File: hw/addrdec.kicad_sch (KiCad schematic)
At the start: 5 parts, among them U10 74AS138, U11 74ACT00P, U5 74AHCT02, U8 74AS04N, U9 74AS27

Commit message: add hw design for veraduino
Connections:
- net DEV0_~{CS} renamed VERA_~{CS}
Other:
- moved on the sheet: U11C, U11E, U5D, U8A, U8G, U9C, U9D

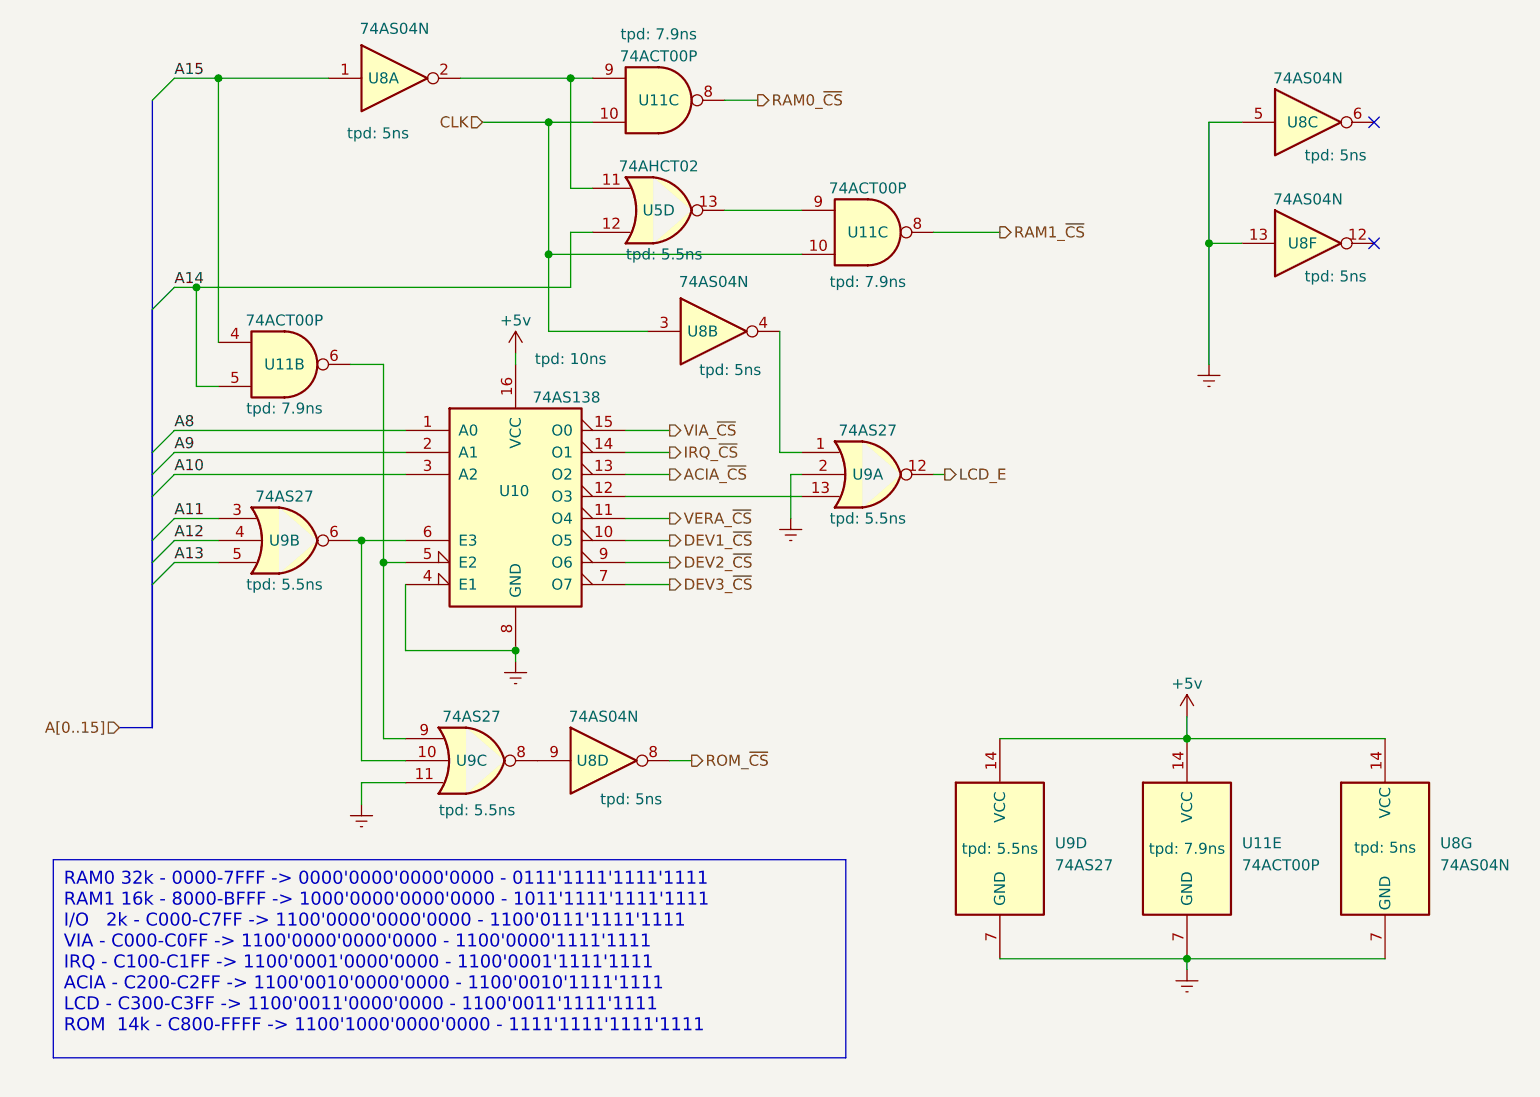
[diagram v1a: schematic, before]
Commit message: add hw schematics for video output with veraduino
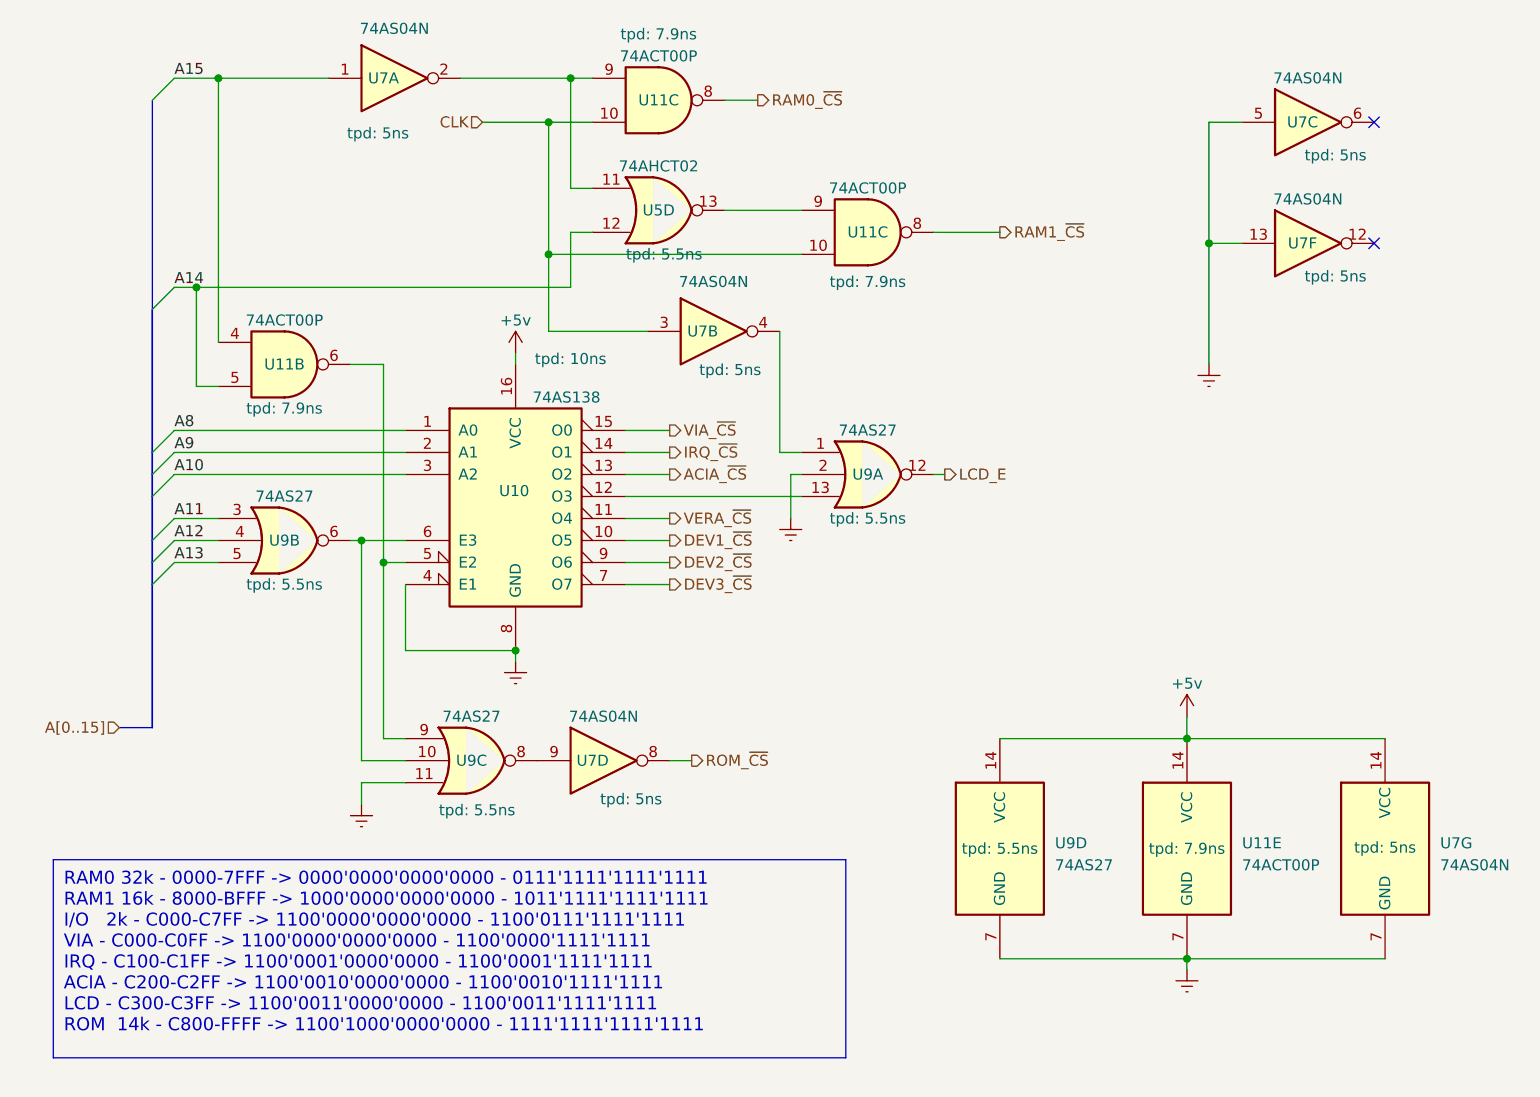
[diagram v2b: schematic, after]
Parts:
- renumbered U8 to U7
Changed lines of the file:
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@@
   (symbol (lib_id "74xx:74LS04") (at 161.29 43.18 0) (unit 6)
     (in_bom yes) (on_board yes) (dnp no)
-    (property "Reference" "U8" (at 160.655 43.18 0)
+    (property "Reference" "U7" (at 160.655 43.18 0)
       (effects (font (size 1.27 1.27)))
     )
@@
       (project "rod6502"
         (path "/031ea57b-8d17-4b45-87cc-c58302485ce1/4032fa43-c28c-4c35-b0ce-d5d9da6e84af"
-          (reference "U8") (unit 6)
+          (reference "U7") (unit 6)
         )
         (path "/031ea57b-8d17-4b45-87cc-c58302485ce1/890f0003-2042-459e-ac4a-1dd81f8fbcc6"
@@
   (symbol (lib_id "74xx:74LS04") (at 161.29 29.21 0) (unit 3)
     (in_bom yes) (on_board yes) (dnp no)
-    (property "Reference" "U8" (at 160.655 29.21 0)
+    (property "Reference" "U7" (at 160.655 29.21 0)
       (effects (font (size 1.27 1.27)))
     )
@@
       (project "rod6502"
         (path "/031ea57b-8d17-4b45-87cc-c58302485ce1/4032fa43-c28c-4c35-b0ce-d5d9da6e84af"
-          (reference "U8") (unit 3)
+          (reference "U7") (unit 3)
         )
         (path "/031ea57b-8d17-4b45-87cc-c58302485ce1/890f0003-2042-459e-ac4a-1dd81f8fbcc6"
@@
         )
         (path "/031ea57b-8d17-4b45-87cc-c58302485ce1/4032fa43-c28c-4c35-b0ce-d5d9da6e84af"
-          (reference "U7") (unit 1)
+          (reference "U8") (unit 1)
         )
       )
@@
   (symbol (lib_id "power:Earth") (at 149.86 57.15 0) (unit 1)
     (in_bom yes) (on_board yes) (dnp no) (fields_autoplaced)
-    (property "Reference" "#PWR044" (at 149.86 63.5 0)
+    (property "Reference" "#PWR018" (at 149.86 63.5 0)
       (effects (font (size 1.27 1.27)) hide)
     )
@@
       (project "rod6502"
         (path "/031ea57b-8d17-4b45-87cc-c58302485ce1/4032fa43-c28c-4c35-b0ce-d5d9da6e84af"
-          (reference "#PWR044") (unit 1)
+          (reference "#PWR018") (unit 1)
         )
       )
@@
   (symbol (lib_id "power:Earth") (at 69.85 91.44 0) (unit 1)
     (in_bom yes) (on_board yes) (dnp no) (fields_autoplaced)
-    (property "Reference" "#PWR024" (at 69.85 97.79 0)
+    (property "Reference" "#PWR020" (at 69.85 97.79 0)
       (effects (font (size 1.27 1.27)) hide)
     )
@@
       (project "rod6502"
         (path "/031ea57b-8d17-4b45-87cc-c58302485ce1/4032fa43-c28c-4c35-b0ce-d5d9da6e84af"
-          (reference "#PWR024") (unit 1)
+          (reference "#PWR020") (unit 1)
         )
       )
@@
   (symbol (lib_id "74xx:74LS04") (at 170.18 113.03 0) (unit 7)
     (in_bom yes) (on_board yes) (dnp no)
-    (property "Reference" "U8" (at 176.53 112.395 0)
+    (property "Reference" "U7" (at 176.53 112.395 0)
       (effects (font (size 1.27 1.27)) (justify left))
     )
@@
       (project "rod6502"
         (path "/031ea57b-8d17-4b45-87cc-c58302485ce1/4032fa43-c28c-4c35-b0ce-d5d9da6e84af"
-          (reference "U8") (unit 7)
+          (reference "U7") (unit 7)
         )
       )
@@
   (symbol (lib_id "power:VCC") (at 147.32 97.79 0) (unit 1)
     (in_bom yes) (on_board yes) (dnp no) (fields_autoplaced)
-    (property "Reference" "#PWR019" (at 147.32 101.6 0)
+    (property "Reference" "#PWR021" (at 147.32 101.6 0)
       (effects (font (size 1.27 1.27)) hide)
     )
@@
       (project "rod6502"
         (path "/031ea57b-8d17-4b45-87cc-c58302485ce1/4032fa43-c28c-4c35-b0ce-d5d9da6e84af"
-          (reference "#PWR019") (unit 1)
+          (reference "#PWR021") (unit 1)
         )
       )
@@
         )
         (path "/031ea57b-8d17-4b45-87cc-c58302485ce1/4032fa43-c28c-4c35-b0ce-d5d9da6e84af"
-          (reference "U7") (unit 5)
+          (reference "U8") (unit 5)
         )
       )
@@
   (symbol (lib_id "power:Earth") (at 101.6 74.93 0) (unit 1)
     (in_bom yes) (on_board yes) (dnp no) (fields_autoplaced)
-    (property "Reference" "#PWR052" (at 101.6 81.28 0)
+    (property "Reference" "#PWR019" (at 101.6 81.28 0)
       (effects (font (size 1.27 1.27)) hide)
     )
@@
       (project "rod6502"
         (path "/031ea57b-8d17-4b45-87cc-c58302485ce1/4032fa43-c28c-4c35-b0ce-d5d9da6e84af"
-          (reference "#PWR052") (unit 1)
+          (reference "#PWR019") (unit 1)
         )
       )
@@
   (symbol (lib_id "74xx:74LS04") (at 55.88 24.13 0) (unit 1)
     (in_bom yes) (on_board yes) (dnp no)
-    (property "Reference" "U8" (at 54.61 24.13 0)
+    (property "Reference" "U7" (at 54.61 24.13 0)
       (effects (font (size 1.27 1.27)))
     )
@@
       (project "rod6502"
         (path "/031ea57b-8d17-4b45-87cc-c58302485ce1/4032fa43-c28c-4c35-b0ce-d5d9da6e84af"
-          (reference "U8") (unit 1)
+          (reference "U7") (unit 1)
         )
       )
@@
   (symbol (lib_id "power:Earth") (at 147.32 127 0) (unit 1)
     (in_bom yes) (on_board yes) (dnp no) (fields_autoplaced)
-    (property "Reference" "#PWR020" (at 147.32 133.35 0)
+    (property "Reference" "#PWR023" (at 147.32 133.35 0)
       (effects (font (size 1.27 1.27)) hide)
     )
@@
       (project "rod6502"
         (path "/031ea57b-8d17-4b45-87cc-c58302485ce1/4032fa43-c28c-4c35-b0ce-d5d9da6e84af"
-          (reference "#PWR020") (unit 1)
+          (reference "#PWR023") (unit 1)
         )
       )
@@
   (symbol (lib_id "power:VCC") (at 69.85 55.88 0) (unit 1)
     (in_bom yes) (on_board yes) (dnp no) (fields_autoplaced)
-    (property "Reference" "#PWR021" (at 69.85 59.69 0)
+    (property "Reference" "#PWR017" (at 69.85 59.69 0)
       (effects (font (size 1.27 1.27)) hide)
     )
@@
       (project "rod6502"
         (path "/031ea57b-8d17-4b45-87cc-c58302485ce1/4032fa43-c28c-4c35-b0ce-d5d9da6e84af"
-          (reference "#PWR021") (unit 1)
+          (reference "#PWR017") (unit 1)
         )
       )
@@
         )
         (path "/031ea57b-8d17-4b45-87cc-c58302485ce1/4032fa43-c28c-4c35-b0ce-d5d9da6e84af"
+          (reference "U8") (unit 2)
+        )
+      )
+    )
+  )
+  (symbol (lib_id "74xx:74LS04") (at 92.71 53.34 0) (unit 2)
+    (in_bom yes) (on_board yes) (dnp no)
+    (property "Reference" "U7" (at 91.44 53.34 0)
+      (effects (font (size 1.27 1.27)))
+    )
+    (property "Value" "74AS04N" (at 92.71 47.625 0)
+      (effects (font (size 1.27 1.27)))
+    )
+    (property "Footprint" "" (at 92.71 53.34 0)
+      (effects (font (size 1.27 1.27)) hide)
+    )
+    (property "Datasheet" "http://www.ti.com/lit/gpn/sn74AS04" (at 92.71 53.34 0)
+      (effects (font (size 1.27 1.27)) hide)
+    )
+    (property "tpd" "5ns" (at 94.615 57.785 0) (show_name)
+      (effects (font (size 1.27 1.27)))
+    )
+    (property "Field5" "" (at 92.71 53.34 0)
+      (effects (font (size 1.27 1.27)) hide)
+    )
+    (pin "1")
+    (pin "2")
+    (pin "3")
+    (pin "4")
+    (pin "5")
+    (pin "6")
+    (pin "8")
+    (pin "9")
+    (pin "10")
+    (pin "11")
+    (pin "12")
+    (pin "13")
+    (pin "14")
+    (pin "7")
+    (instances
+      (project "rod6502"
+        (path "/031ea57b-8d17-4b45-87cc-c58302485ce1/4032fa43-c28c-4c35-b0ce-d5d9da6e84af"
           (reference "U7") (unit 2)
-        )
-      )
-    )
-  )
-  (symbol (lib_id "74xx:74LS04") (at 92.71 53.34 0) (unit 2)
-    (in_bom yes) (on_board yes) (dnp no)
-    (property "Reference" "U8" (at 91.44 53.34 0)
-      (effects (font (size 1.27 1.27)))
-    )
-    (property "Value" "74AS04N" (at 92.71 47.625 0)
-      (effects (font (size 1.27 1.27)))
-    )
-    (property "Footprint" "" (at 92.71 53.34 0)
-      (effects (font (size 1.27 1.27)) hide)
-    )
-    (property "Datasheet" "http://www.ti.com/lit/gpn/sn74AS04" (at 92.71 53.34 0)
-      (effects (font (size 1.27 1.27)) hide)
-    )
-    (property "tpd" "5ns" (at 94.615 57.785 0) (show_name)
-      (effects (font (size 1.27 1.27)))
-    )
-    (property "Field5" "" (at 92.71 53.34 0)
-      (effects (font (size 1.27 1.27)) hide)
-    )
-    (pin "1")
-    (pin "2")
-    (pin "3")
-    (pin "4")
-    (pin "5")
-    (pin "6")
-    (pin "8")
-    (pin "9")
-    (pin "10")
-    (pin "11")
-    (pin "12")
-    (pin "13")
-    (pin "14")
-    (pin "7")
-    (instances
-      (project "rod6502"
-        (path "/031ea57b-8d17-4b45-87cc-c58302485ce1/4032fa43-c28c-4c35-b0ce-d5d9da6e84af"
-          (reference "U8") (unit 2)
         )
       )
@@
         )
         (path "/031ea57b-8d17-4b45-87cc-c58302485ce1/4032fa43-c28c-4c35-b0ce-d5d9da6e84af"
-          (reference "U7") (unit 4)
+          (reference "U8") (unit 4)
         )
       )
@@
   (symbol (lib_id "74xx:74LS04") (at 80.01 102.87 0) (unit 4)
     (in_bom yes) (on_board yes) (dnp no)
-    (property "Reference" "U8" (at 78.74 102.87 0)
+    (property "Reference" "U7" (at 78.74 102.87 0)
       (effects (font (size 1.27 1.27)))
     )
@@
       (project "rod6502"
         (path "/031ea57b-8d17-4b45-87cc-c58302485ce1/4032fa43-c28c-4c35-b0ce-d5d9da6e84af"
-          (reference "U8") (unit 4)
-        )
-      )
+          (reference "U7") (unit 4)
+        )
+      )

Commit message: clean up hw schematics
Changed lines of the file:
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@@
     (stroke (width 0) (type default))
   )
-  (text_box "RAM0 32k - 0000-7FFF -> 0000'0000'0000'0000 - 0111'1111'1111'1111\nRAM1 16k - 8000-BFFF -> 1000'0000'0000'0000 - 1011'1111'1111'1111\nI/O   2k - C000-C7FF -> 1100'0000'0000'0000 - 1100'0111'1111'1111\n     VIA - C000-C0FF -> 1100'0000'0000'0000 - 1100'0000'1111'1111\n     IRQ - C100-C1FF -> 1100'0001'0000'0000 - 1100'0001'1111'1111\n    ACIA - C200-C2FF -> 1100'0010'0000'0000 - 1100'0010'1111'1111\n     LCD - C300-C3FF -> 1100'0011'0000'0000 - 1100'0011'1111'1111\nROM  14k - C800-FFFF -> 1100'1000'0000'0000 - 1111'1111'1111'1111\n"
-    (at 16.51 114.3 0) (size 91.44 22.86)
+  (text_box "RAM0 32k - 0000-7FFF -> 0000'0000'0000'0000 - 0111'1111'1111'1111\nRAM1 16k - 8000-BFFF -> 1000'0000'0000'0000 - 1011'1111'1111'1111\nI/O   2k - C000-C7FF -> 1100'0000'0000'0000 - 1100'0111'1111'1111\n     VIA - C000-C0FF -> 1100'0000'0000'0000 - 1100'0000'1111'1111\n     IRQ - C100-C1FF -> 1100'0001'0000'0000 - 1100'0001'1111'1111\n    ACIA - C200-C2FF -> 1100'0010'0000'0000 - 1100'0010'1111'1111\n     LCD - C300-C3FF -> 1100'0011'0000'0000 - 1100'0011'1111'1111\n    VERA - C400-C4FF -> 1100'0100'0000'0000 - 1100'0100'1111'1111\nROM  14k - C800-FFFF -> 1100'1000'0000'0000 - 1111'1111'1111'1111\n"
+    (at 16.51 114.3 0) (size 91.44 25.4)
     (stroke (width 0) (type default))
     (fill (type none))
